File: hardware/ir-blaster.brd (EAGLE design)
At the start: 85.1 x 55.9 mm, 10 parts, among them Q1 BC547

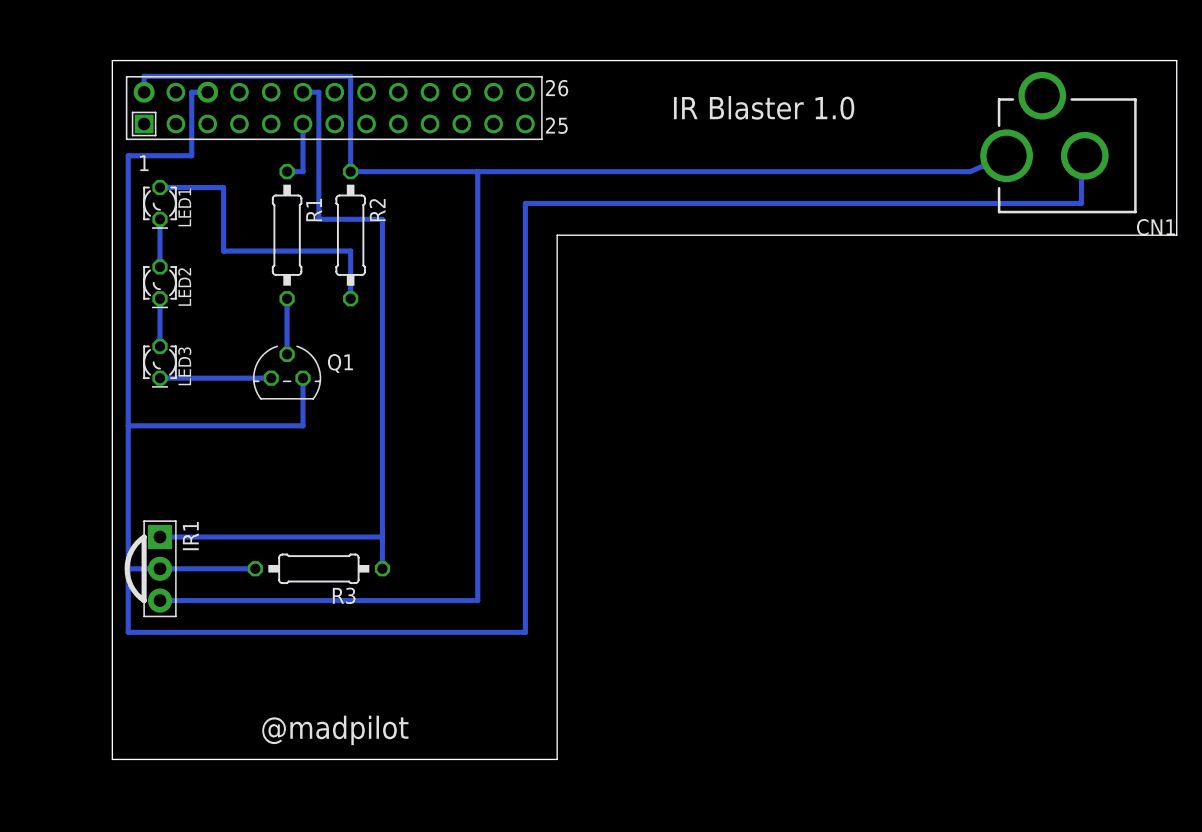
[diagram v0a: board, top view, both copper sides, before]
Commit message: Redesigning board so it fits on top of the PI properly
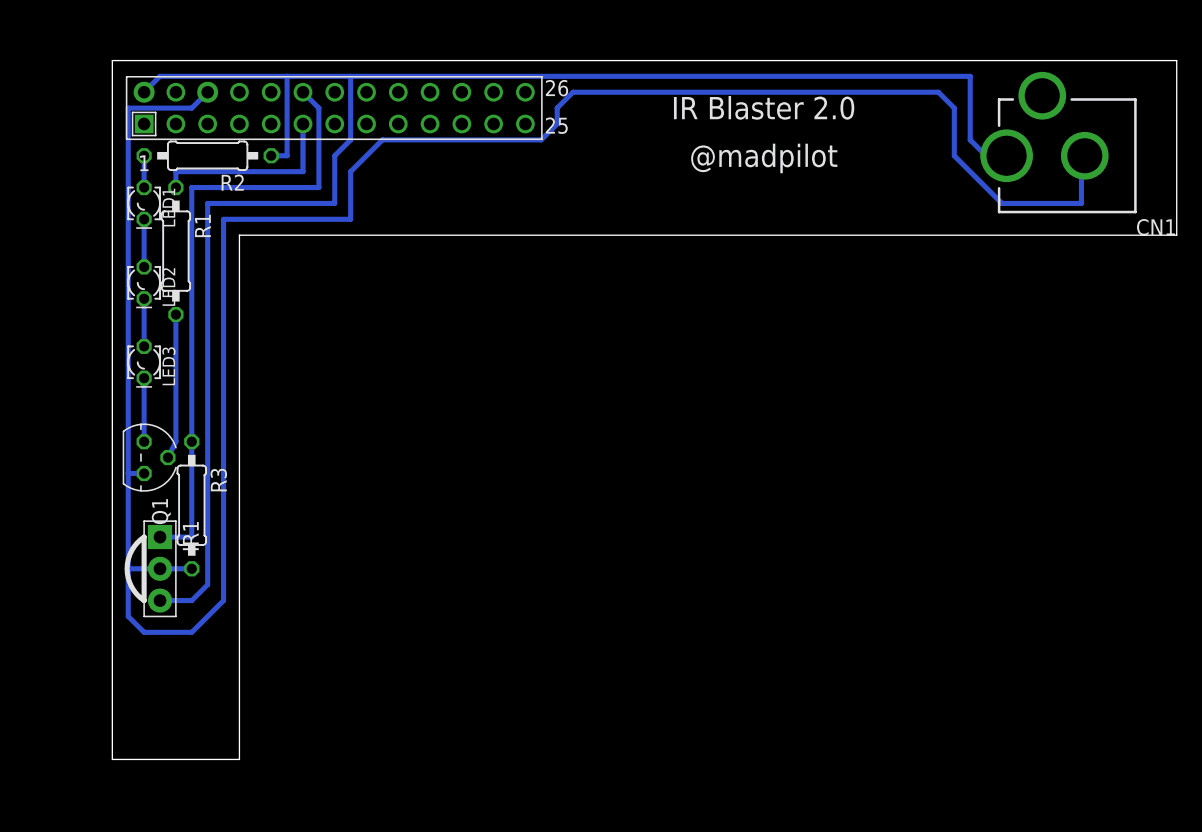
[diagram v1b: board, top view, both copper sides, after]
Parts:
- moved Q1 13.1 mm to (2.54, 24.1), turned to 270 degrees
- moved R2 13.1 mm to (7.62, 48.3), turned to 180 degrees
- moved R3 11.4 mm to (6.35, 20.3), turned to 270 degrees
- moved R1 8.98 mm to (5.08, 40.6)
- moved LED1 1.27 mm to (2.54, 44.5)
- moved LED2 1.27 mm to (2.54, 38.1)
- moved LED3 1.27 mm to (2.54, 31.8)
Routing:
- net N$2: track 24.1 -> 2.54 mm
- net N$7: track 62.2 -> 48.8 mm
- net GND: track 192.0 -> 179.3 mm
- net N$6: track 5.08 -> 15.2 mm
- net N$5: track 4.45 -> 11.6 mm
- net N$1: track 8.89 -> 5.08 mm
- net VCC: track 137.8 -> 138.4 mm
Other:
- outline, holes or cut-outs redrawn
- board text added: "IR Blaster 2.0"
- board text removed: "IR Blaster 1.0"

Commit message: Revision 3. Moved the LEDs off board onto wires
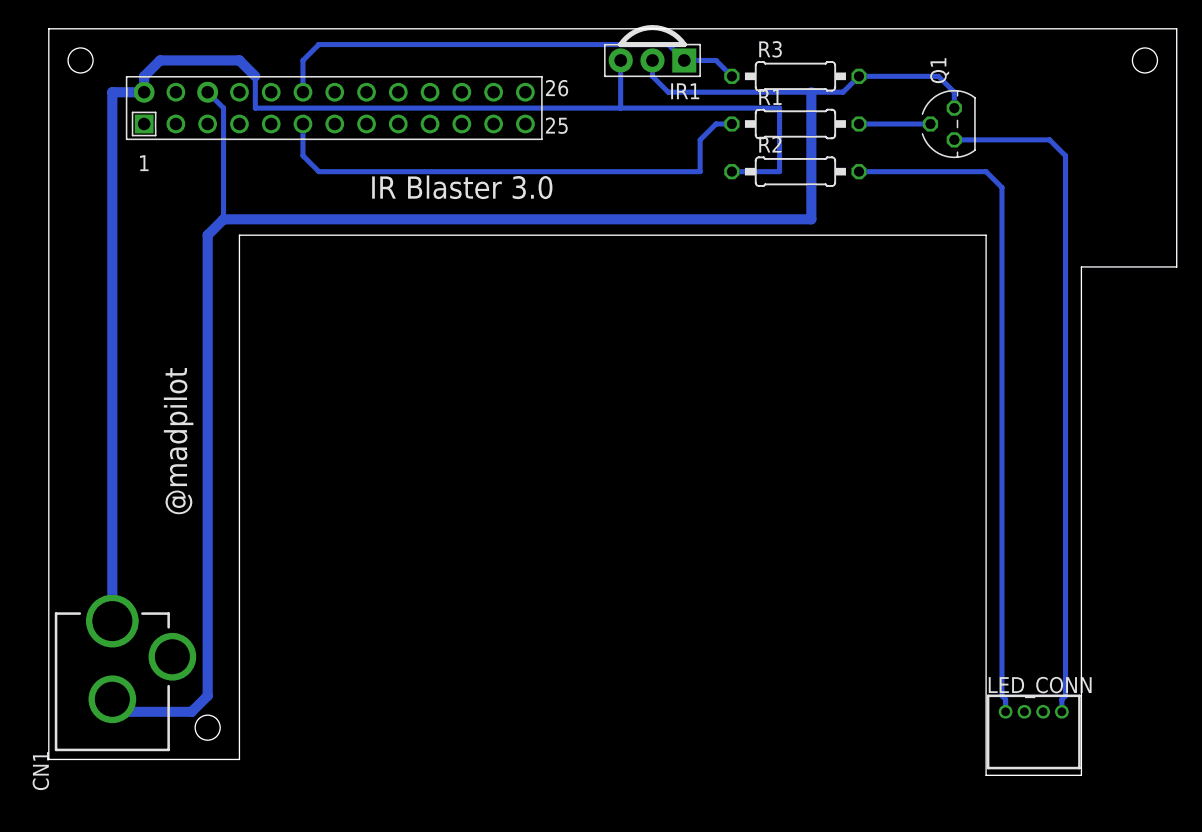
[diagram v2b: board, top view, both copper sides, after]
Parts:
- removed LED1, LED2, LED3: IR, eagle-ltspice:LED_LD260
- added LED_CONN: S4B-ZR, con-jst:S4B-ZR
- R1: value 1k -> 1.8k
- moved CN1 99.1 mm to (0.00, -2.54), turned to 0 degrees
- moved Q1 70.0 mm to (67.3, 50.8), turned to 90 degrees
- moved R3 59.2 mm to (54.6, 54.6), turned to 0 degrees
- moved IR1 56.6 mm to (43.2, 55.9), turned to 180 degrees
- moved R1 50.6 mm to (54.6, 50.8), turned to 0 degrees
- moved R2 47.0 mm to (54.6, 47.0), turned to 0 degrees
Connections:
- removed net N$3: LED1.K, LED2.A
- removed net N$4: LED2.K, LED3.A
- net N$1: now also LED_CONN.1, R2.2; no longer LED3.K, Q1.3
- net N$2: now also LED_CONN.4, Q1.3; no longer LED1.A, R2.2
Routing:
- net N$2: track 2.54 -> 54.0 mm
- net N$1: track 5.08 -> 54.0 mm
- net GND: track 179.3 -> 143.2 mm
- net N$6: track 15.2 -> 40.4 mm
- net VCC: track 138.4 -> 113.2 mm
- net N$7: track 48.8 -> 38.4 mm
- net N$5: track 11.6 -> 5.72 mm
- net N$3: track 3.81 -> 0.00 mm
- net N$4: track 3.81 -> 0.00 mm
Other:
- board size 85.1 x 55.9 mm -> 90.2 x 59.7 mm
- board text added: "IR Blaster 3.0"
- board text removed: "IR Blaster 2.0"

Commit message: Flipping board, so screw holes align of three of the four corners
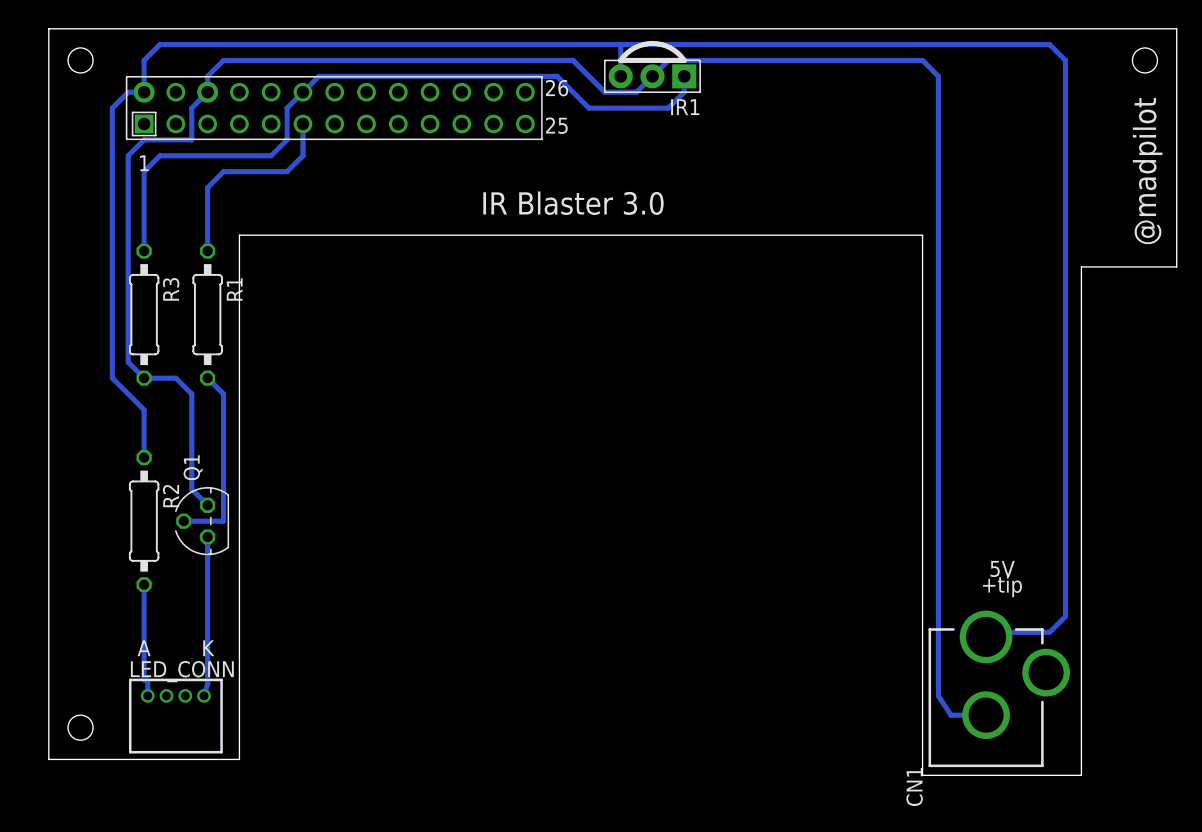
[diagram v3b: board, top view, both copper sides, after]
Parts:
- moved CN1 69.9 mm to (69.8, -3.81)
- moved LED_CONN 68.6 mm to (5.08, 5.08)
- moved Q1 67.6 mm to (7.62, 19.1)
- moved R2 59.1 mm to (2.54, 19.1), turned to 270 degrees
- moved R3 55.4 mm to (2.54, 35.6), turned to 270 degrees
- moved R1 49.4 mm to (7.62, 35.6), turned to 270 degrees
- moved IR1 1.27 mm to (43.2, 54.6)
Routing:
- net VCC: track 113.2 -> 163.3 mm
- net N$1: track 54.0 -> 9.18 mm
- net N$2: track 54.0 -> 12.7 mm
- net N$6: track 40.4 -> 16.3 mm
- net N$7: track 38.4 -> 57.0 mm
- net GND: track 143.2 -> 159.0 mm
- net N$5: track 5.72 -> 15.1 mm
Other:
- outline, holes or cut-outs redrawn
- board text added: "+tip"
- board text added: "5V"
- board text added: "A"
- board text added: "K"

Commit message: Adjusted screw hold position to match ethernet port holes. Reduced width of board so USB network adapter will fit. Adjusted labels to fit on board
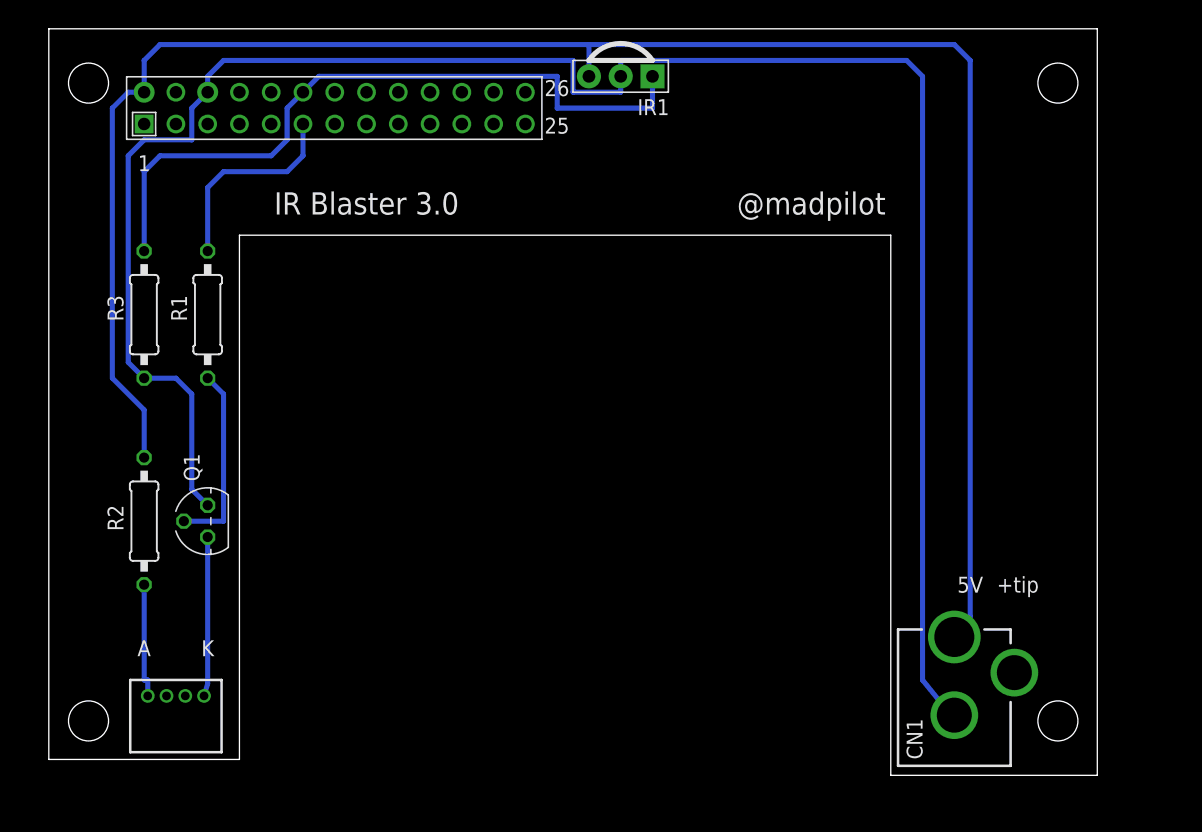
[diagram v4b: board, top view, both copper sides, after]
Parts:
- moved IR1 2.54 mm to (40.6, 54.6)
- moved CN1 2.54 mm to (67.3, -3.81)
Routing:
- net VCC: track 163.3 -> 150.8 mm
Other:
- board size 90.2 x 59.7 mm -> 83.8 x 59.7 mm
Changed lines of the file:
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@@
 <wire x1="-5.08" y1="0" x2="10.16" y2="0" width="0" layer="20"/>
 <wire x1="10.16" y1="0" x2="10.16" y2="41.91" width="0" layer="20"/>
-<wire x1="10.16" y1="41.91" x2="64.77" y2="41.91" width="0" layer="20"/>
-<wire x1="64.77" y1="41.91" x2="64.77" y2="-1.27" width="0" layer="20"/>
-<wire x1="64.77" y1="-1.27" x2="77.47" y2="-1.27" width="0" layer="20"/>
-<wire x1="77.47" y1="-1.27" x2="77.47" y2="39.37" width="0" layer="20"/>
-<wire x1="77.47" y1="39.37" x2="85.09" y2="39.37" width="0" layer="20"/>
-<wire x1="85.09" y1="39.37" x2="85.09" y2="58.41" width="0" layer="20"/>
-<wire x1="85.09" y1="58.41" x2="-5.08" y2="58.41" width="0" layer="20"/>
+<wire x1="10.16" y1="41.91" x2="62.23" y2="41.91" width="0" layer="20"/>
+<wire x1="62.23" y1="41.91" x2="62.23" y2="-1.27" width="0" layer="20"/>
+<wire x1="62.23" y1="-1.27" x2="78.74" y2="-1.27" width="0" layer="20"/>
+<wire x1="78.74" y1="-1.27" x2="78.74" y2="58.41" width="0" layer="20"/>
+<wire x1="78.74" y1="58.41" x2="-5.08" y2="58.41" width="0" layer="20"/>
 <wire x1="-5.08" y1="58.41" x2="-5.08" y2="0" width="0" layer="20"/>
-<text x="82.55" y="46.99" size="1.778" layer="21" font="vector" rot="R270" align="center">@madpilot</text>
-<text x="36.83" y="44.45" size="1.778" layer="21" font="vector" align="center">IR Blaster 3.0</text>
-<hole x="-2.54" y="55.88" drill="2"/>
-<hole x="-2.54" y="2.54" drill="2"/>
-<hole x="82.55" y="55.88" drill="2"/>
-<text x="71.12" y="13.97" size="1.27" layer="21" font="fixed" align="center">+tip</text>
-<text x="71.12" y="15.24" size="1.27" layer="21" font="fixed" align="center">5V</text>
+<text x="55.88" y="44.45" size="1.778" layer="21" font="vector" align="center">@madpilot</text>
+<text x="20.32" y="44.45" size="1.778" layer="21" font="vector" align="center">IR Blaster 3.0</text>
+<hole x="-1.905" y="54.07" drill="3.2"/>
+<hole x="-1.905" y="3.08" drill="3.2"/>
+<hole x="75.58999375" y="54.07" drill="3.2"/>
+<text x="72.39" y="13.97" size="1.27" layer="21" font="fixed" align="center">+tip</text>
+<text x="68.58" y="13.97" size="1.27" layer="21" font="fixed" align="center">5V</text>
 <text x="2.54" y="8.89" size="1.27" layer="21" font="fixed" align="center">A</text>
 <text x="7.62" y="8.89" size="1.27" layer="21" font="fixed" align="center">K</text>
+<hole x="75.58999375" y="3.08" drill="3.2"/>
 </plain>
 <attributes>
@@
 </autorouter>
 <elements>
-<element name="R1" library="eagle-ltspice" package="0207/10" value="1.8k" x="7.62" y="35.56" rot="R270">
+<element name="R1" library="eagle-ltspice" package="0207/10" value="1.8k" x="7.62" y="35.56" smashed="yes" rot="R270">
+<attribute name="NAME" x="5.334" y="36.068" size="1.27" layer="25" ratio="10" rot="R270" align="center"/>
 <attribute name="SPICEMODEL" value="NONE" x="7.62" y="35.56" size="1.778" layer="27" rot="R270" display="off"/>
 <attribute name="SPICEPREFIX" value="R" x="7.62" y="35.56" size="1.778" layer="27" rot="R270" display="off"/>
-</element>
-<element name="R2" library="eagle-ltspice" package="0207/10" value="56" x="2.54" y="19.05" rot="R270">
+<attribute name="VALUE" x="6.985" y="37.8206" size="1.27" layer="27" ratio="10" rot="R270"/>
+</element>
+<element name="R2" library="eagle-ltspice" package="0207/10" value="56" x="2.54" y="19.05" smashed="yes" rot="R270">
+<attribute name="NAME" x="0.254" y="19.304" size="1.27" layer="25" ratio="10" rot="R270" align="center"/>
 <attribute name="SPICEMODEL" value="NONE" x="2.54" y="19.05" size="1.778" layer="27" rot="R270" display="off"/>
 <attribute name="SPICEPREFIX" value="R" x="2.54" y="19.05" size="1.778" layer="27" rot="R270" display="off"/>
+<attribute name="VALUE" x="1.905" y="21.3106" size="1.27" layer="27" ratio="10" rot="R270"/>
 </element>
 <element name="Q1" library="transistor" package="TO92" value="BC547" x="7.62" y="19.05" rot="R90"/>
-<element name="IR1" library="adafruit" package="PNA460XM" value="RPM7100" x="43.18" y="54.61" rot="R180"/>
-<element name="R3" library="eagle-ltspice" package="0207/10" value="39k" x="2.54" y="35.56" rot="R270">
+<element name="IR1" library="adafruit" package="PNA460XM" value="RPM7100" x="40.64" y="54.61" rot="R180"/>
+<element name="R3" library="eagle-ltspice" package="0207/10" value="39k" x="2.54" y="35.56" smashed="yes" rot="R270">
+<attribute name="NAME" x="0.254" y="36.068" size="1.27" layer="25" ratio="10" rot="R270" align="center"/>
 <attribute name="SPICEMODEL" value="NONE" x="2.54" y="35.56" size="1.778" layer="27" rot="R270" display="off"/>
 <attribute name="SPICEPREFIX" value="R" x="2.54" y="35.56" size="1.778" layer="27" rot="R270" display="off"/>
+<attribute name="VALUE" x="1.905" y="37.8206" size="1.27" layer="27" ratio="10" rot="R270"/>
 </element>
 <element name="U$1" library="RaspberryPi" package="RASPBERRY-PI_REV1" value="RASPBERRY-PI_REV1" x="44.45" y="29.21" smashed="yes"/>
-<element name="CN1" library="adafruit" package="DCJACK_2MM_PTH" value="" x="69.85" y="-3.81"/>
-<element name="LED_CONN" library="con-jst" package="S4B-ZR" value="S4B-ZR" x="5.08" y="5.08">
+<element name="CN1" library="adafruit" package="DCJACK_2MM_PTH" value="" x="67.31" y="-3.81" smashed="yes">
+<attribute name="NAME" x="64.77" y="0" size="1.27" layer="25" rot="R90"/>
+<attribute name="VALUE" x="73.66" y="-3.81" size="1.27" layer="27" rot="R90"/>
+</element>
+<element name="LED_CONN" library="con-jst" package="S4B-ZR" value="S4B-ZR" x="5.08" y="5.08" smashed="yes">
 <attribute name="MF" value="FARNELL" x="5.08" y="5.08" size="1.778" layer="27" display="off"/>
 <attribute name="MPN" value="S4B-ZR(LF)(SN)" x="5.08" y="5.08" size="1.778" layer="27" display="off"/>
 <attribute name="OC_FARNELL" value="9491830" x="5.08" y="5.08" size="1.778" layer="27" display="off"/>
 <attribute name="OC_NEWARK" value="38K8076" x="5.08" y="5.08" size="1.778" layer="27" display="off"/>
+<attribute name="VALUE" x="2.54" y="1.27" size="1.27" layer="27"/>
 </element>
 </elements>
@@
 <wire x1="7.62" y1="54.61" x2="8.89" y2="55.88" width="0.4064" layer="16"/>
 <wire x1="8.89" y1="55.88" x2="36.83" y2="55.88" width="0.4064" layer="16"/>
-<wire x1="36.83" y1="55.88" x2="39.37" y2="53.34" width="0.4064" layer="16"/>
-<wire x1="39.37" y1="53.34" x2="41.91" y2="53.34" width="0.4064" layer="16"/>
-<wire x1="41.91" y1="53.34" x2="43.18" y2="54.61" width="0.4064" layer="16"/>
-<wire x1="44.45" y1="55.88" x2="43.18" y2="54.61" width="0.4064" layer="16"/>
-<wire x1="69.85" y1="3.54" x2="67.04" y2="3.54" width="0.4064" layer="16"/>
-<wire x1="67.04" y1="3.54" x2="66.04" y2="5.08" width="0.4064" layer="16"/>
-<wire x1="66.04" y1="5.08" x2="66.04" y2="54.61" width="0.4064" layer="16"/>
-<wire x1="66.04" y1="54.61" x2="64.77" y2="55.88" width="0.4064" layer="16"/>
-<wire x1="64.77" y1="55.88" x2="44.45" y2="55.88" width="0.4064" layer="16"/>
+<wire x1="36.83" y1="55.88" x2="36.83" y2="53.34" width="0.4064" layer="16"/>
+<wire x1="36.83" y1="53.34" x2="40.64" y2="53.34" width="0.4064" layer="16"/>
+<wire x1="40.64" y1="53.34" x2="40.64" y2="54.61" width="0.4064" layer="16"/>
+<wire x1="40.64" y1="55.88" x2="40.64" y2="54.61" width="0.4064" layer="16"/>
+<wire x1="67.31" y1="3.54" x2="67.04" y2="3.54" width="0.4064" layer="16"/>
+<wire x1="67.04" y1="3.54" x2="64.77" y2="6.35" width="0.4064" layer="16"/>
+<wire x1="64.77" y1="6.35" x2="64.77" y2="54.61" width="0.4064" layer="16"/>
+<wire x1="64.77" y1="54.61" x2="63.5" y2="55.88" width="0.4064" layer="16"/>
+<wire x1="63.5" y1="55.88" x2="40.64" y2="55.88" width="0.4064" layer="16"/>
 </signal>
 <signal name="VCC">
@@
 <wire x1="2.54" y1="53.34" x2="2.54" y2="55.88" width="0.4064" layer="16"/>
 <wire x1="2.54" y1="55.88" x2="3.81" y2="57.15" width="0.4064" layer="16"/>
-<wire x1="3.81" y1="57.15" x2="40.64" y2="57.15" width="0.4064" layer="16"/>
-<wire x1="40.64" y1="54.61" x2="40.64" y2="57.15" width="0.4064" layer="16"/>
-<wire x1="40.64" y1="57.15" x2="74.93" y2="57.15" width="0.4064" layer="16"/>
-<wire x1="74.93" y1="57.15" x2="76.2" y2="55.88" width="0.4064" layer="16"/>
-<wire x1="76.2" y1="55.88" x2="76.2" y2="11.43" width="0.4064" layer="16"/>
-<wire x1="76.2" y1="11.43" x2="74.93" y2="10.16" width="0.4064" layer="16"/>
-<wire x1="74.93" y1="10.16" x2="70.22" y2="10.16" width="0.4064" layer="16"/>
-<wire x1="70.22" y1="10.16" x2="69.85" y2="9.79" width="0.4064" layer="16"/>
+<wire x1="3.81" y1="57.15" x2="38.1" y2="57.15" width="0.4064" layer="16"/>
+<wire x1="38.1" y1="54.61" x2="38.1" y2="57.15" width="0.4064" layer="16"/>
+<wire x1="38.1" y1="57.15" x2="67.31" y2="57.15" width="0.4064" layer="16"/>
+<wire x1="67.31" y1="57.15" x2="68.58" y2="55.88" width="0.4064" layer="16"/>
+<wire x1="68.58" y1="55.88" x2="68.58" y2="11.43" width="0.4064" layer="16"/>
+<wire x1="68.58" y1="11.43" x2="67.68" y2="10.16" width="0.4064" layer="16"/>
+<wire x1="67.68" y1="10.16" x2="67.31" y2="9.79" width="0.4064" layer="16"/>
 </signal>
 <signal name="N$7">
@@
 <wire x1="15.24" y1="53.34" x2="16.51" y2="54.61" width="0.4064" layer="16"/>
 <wire x1="16.51" y1="54.61" x2="35.56" y2="54.61" width="0.4064" layer="16"/>
-<wire x1="35.56" y1="54.61" x2="38.1" y2="52.07" width="0.4064" layer="16"/>
-<wire x1="38.1" y1="52.07" x2="44.45" y2="52.07" width="0.4064" layer="16"/>
-<wire x1="44.45" y1="52.07" x2="45.72" y2="53.34" width="0.4064" layer="16"/>
-<wire x1="45.72" y1="53.34" x2="45.72" y2="54.61" width="0.4064" layer="16"/>
+<wire x1="35.56" y1="54.61" x2="35.56" y2="52.07" width="0.4064" layer="16"/>
+<wire x1="35.56" y1="52.07" x2="43.18" y2="52.07" width="0.4064" layer="16"/>
+<wire x1="43.18" y1="52.07" x2="43.18" y2="54.61" width="0.4064" layer="16"/>
 </signal>
 <signal name="N$5">
